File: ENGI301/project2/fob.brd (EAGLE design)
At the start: 101.6 x 100 mm, 21 parts, among them SW1 PUSH_BUTTON, SW2 PUSH_BUTTON, SW3 PUSH_BUTTON, SW4 PUSH_BUTTON

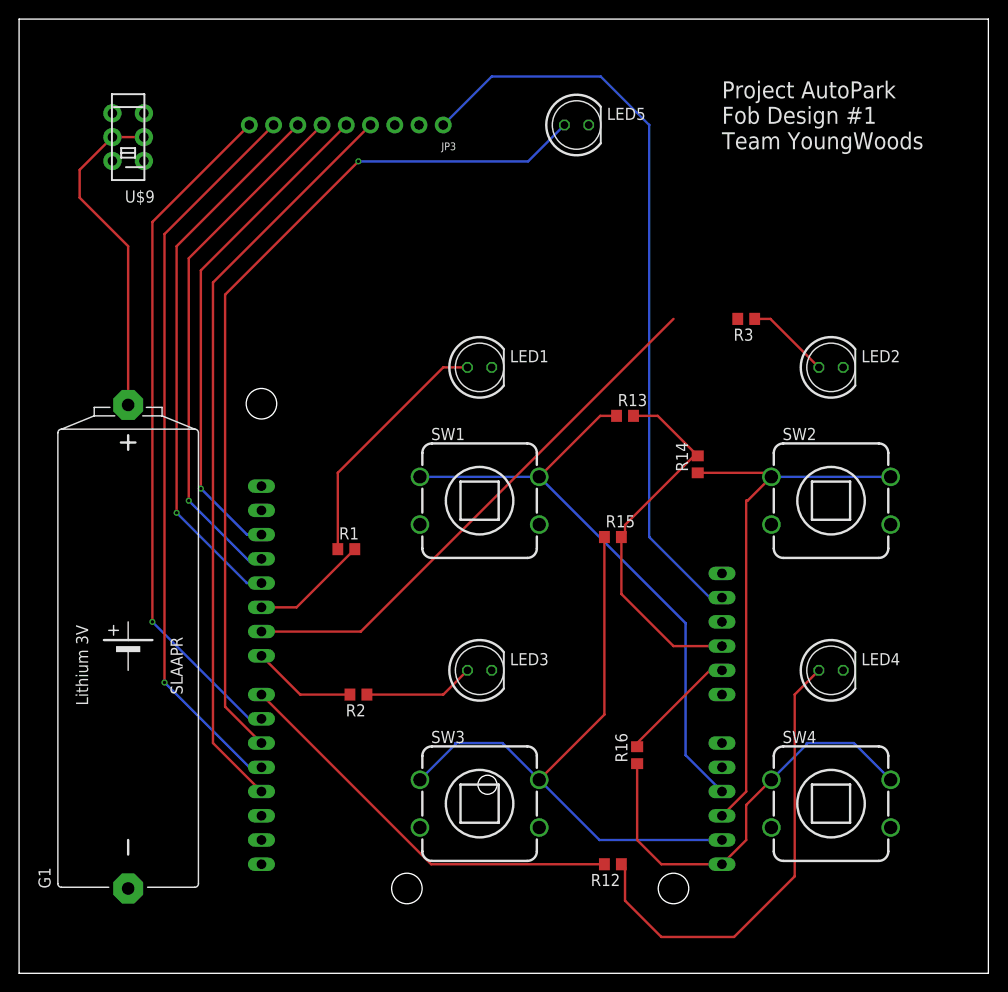
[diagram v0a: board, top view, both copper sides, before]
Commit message: added to PCB design
- mounting holes
- documentation
- titles and stuff
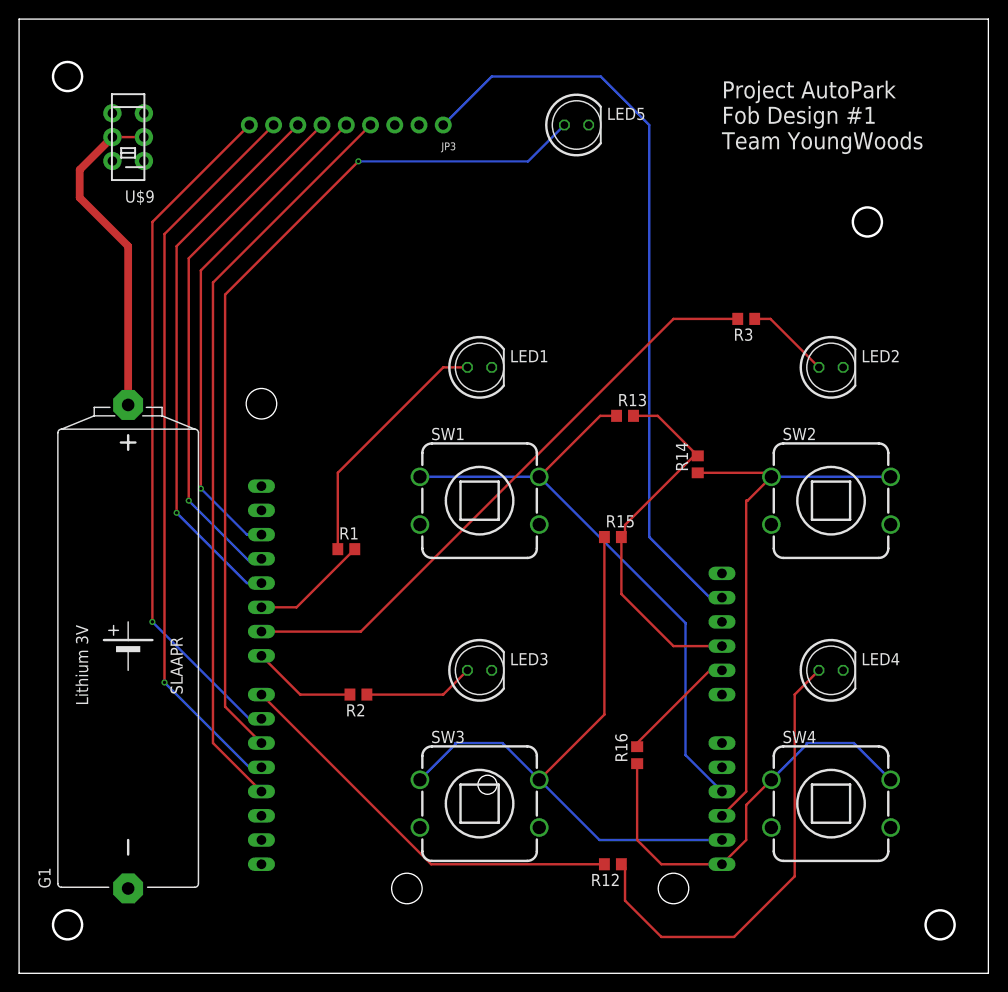
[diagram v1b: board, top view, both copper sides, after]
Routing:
- net L2: track 56.8 -> 63.5 mm
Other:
- outline, holes or cut-outs redrawn
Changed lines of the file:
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@@
 <layers>
 <layer number="1" name="Top" color="4" fill="1" visible="yes" active="yes"/>
-<layer number="2" name="Route2" color="16" fill="1" visible="no" active="yes"/>
+<layer number="2" name="Route2" color="16" fill="1" visible="yes" active="yes"/>
 <layer number="3" name="Route3" color="17" fill="1" visible="no" active="no"/>
 <layer number="4" name="Route4" color="18" fill="1" visible="no" active="no"/>
@@
 <layer number="13" name="Route13" color="21" fill="1" visible="no" active="no"/>
 <layer number="14" name="Route14" color="22" fill="1" visible="no" active="no"/>
-<layer number="15" name="Route15" color="23" fill="1" visible="no" active="yes"/>
+<layer number="15" name="Route15" color="23" fill="1" visible="yes" active="yes"/>
 <layer number="16" name="Bottom" color="1" fill="1" visible="yes" active="yes"/>
 <layer number="17" name="Pads" color="2" fill="1" visible="yes" active="yes"/>
@@
 Fob Design #1
 Team YoungWoods</text>
+<circle x="88.9" y="78.74" radius="1.524" width="0.254" layer="20"/>
+<circle x="96.52" y="5.08" radius="1.524" width="0.254" layer="20"/>
+<circle x="5.08" y="5.08" radius="1.524" width="0.254" layer="20"/>
+<circle x="5.08" y="93.98" radius="1.524" width="0.254" layer="20"/>
+<dimension x1="101.58" y1="0" x2="101.58" y2="100" x3="115.57" y3="50" textsize="1.778" layer="20"/>
+<dimension x1="0" y1="0" x2="101.58" y2="0" x3="50.79" y3="-15.24" textsize="1.778" layer="20"/>
+<dimension x1="6.604" y1="5.08" x2="3.556" y2="5.08" x3="5.08" y3="2.54" textsize="1.778" layer="1" dtype="diameter"/>
+<dimension x1="94.996" y1="5.08" x2="98.044" y2="5.08" x3="96.52" y3="7.62" textsize="1.778" layer="1" dtype="diameter"/>
+<dimension x1="39.37" y1="6.35" x2="39.37" y2="74.93" x3="-5.08" y3="40.64" textsize="1.778" layer="20"/>
+<dimension x1="11.43" y1="59.563" x2="11.43" y2="8.89" x3="0" y3="34.2265" textsize="1.778" layer="20"/>
 </plain>
 <attributes>
@@
 <contactref element="R3" pad="2"/>
 <contactref element="IC1" pad="22"/>
-<wire x1="68.58" y1="68.58" x2="75.311" y2="68.58" width="0" layer="19" extent="1-1"/>
 <wire x1="25.4" y1="35.814" x2="35.814" y2="35.814" width="0.254" layer="1"/>
 <wire x1="35.814" y1="35.814" x2="68.58" y2="68.58" width="0.254" layer="1"/>
+<wire x1="68.58" y1="68.58" x2="75.311" y2="68.58" width="0.254" layer="1"/>
 </signal>
 <signal name="L5">
@@
 <contactref element="U$9" pad="2"/>
 <contactref element="U$9" pad="5"/>
-<wire x1="11.43" y1="59.563" x2="11.43" y2="76.2" width="0.254" layer="1"/>
-<wire x1="11.43" y1="76.2" x2="6.35" y2="81.28" width="0.254" layer="1"/>
-<wire x1="6.35" y1="81.28" x2="6.35" y2="84.2" width="0.254" layer="1"/>
-<wire x1="6.35" y1="84.2" x2="9.78" y2="87.63" width="0.254" layer="1"/>
+<wire x1="11.43" y1="59.563" x2="11.43" y2="76.2" width="0.8128" layer="1"/>
+<wire x1="11.43" y1="76.2" x2="6.35" y2="81.28" width="0.8128" layer="1"/>
+<wire x1="6.35" y1="81.28" x2="6.35" y2="84.2" width="0.8128" layer="1"/>
+<wire x1="6.35" y1="84.2" x2="9.78" y2="87.63" width="0.8128" layer="1"/>
 <wire x1="13.08" y1="87.63" x2="9.78" y2="87.63" width="0.254" layer="1"/>
 </signal>

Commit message: Added gbr files
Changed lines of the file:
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@@
 <board>
 <plain>
-<wire x1="0" y1="0" x2="101.58" y2="0" width="0" layer="20"/>
-<wire x1="101.58" y1="0" x2="101.58" y2="100" width="0" layer="20"/>
-<wire x1="101.58" y1="100" x2="0" y2="100" width="0" layer="20"/>
+<wire x1="0" y1="0" x2="101.6" y2="0" width="0" layer="20"/>
+<wire x1="101.6" y1="0" x2="101.6" y2="100" width="0" layer="20"/>
+<wire x1="101.6" y1="100" x2="0" y2="100" width="0" layer="20"/>
 <wire x1="0" y1="100" x2="0" y2="0" width="0" layer="20"/>
 <text x="73.66" y="86.36" size="1.778" layer="21">Project AutoPark
@@
 <dimension x1="6.604" y1="5.08" x2="3.556" y2="5.08" x3="5.08" y3="2.54" textsize="1.778" layer="1" dtype="diameter"/>
 <dimension x1="94.996" y1="5.08" x2="98.044" y2="5.08" x3="96.52" y3="7.62" textsize="1.778" layer="1" dtype="diameter"/>
-<dimension x1="39.37" y1="6.35" x2="39.37" y2="74.93" x3="-5.08" y3="40.64" textsize="1.778" layer="20"/>
-<dimension x1="11.43" y1="59.563" x2="11.43" y2="8.89" x3="0" y3="34.2265" textsize="1.778" layer="20"/>
 </plain>
 <attributes>
